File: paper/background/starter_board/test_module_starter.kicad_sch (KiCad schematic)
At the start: 14 parts, among them J1 Barrel_Jack_12V, M1 ERM_Motor, M2 Stepper_4wire, M3 Servo_3pin, U1 D24V22F5_Buck, U2 Pi_Pico_W, U3 DRV2605L_Breakout, U4 DRV8871_Breakout, U5 Tic_T500

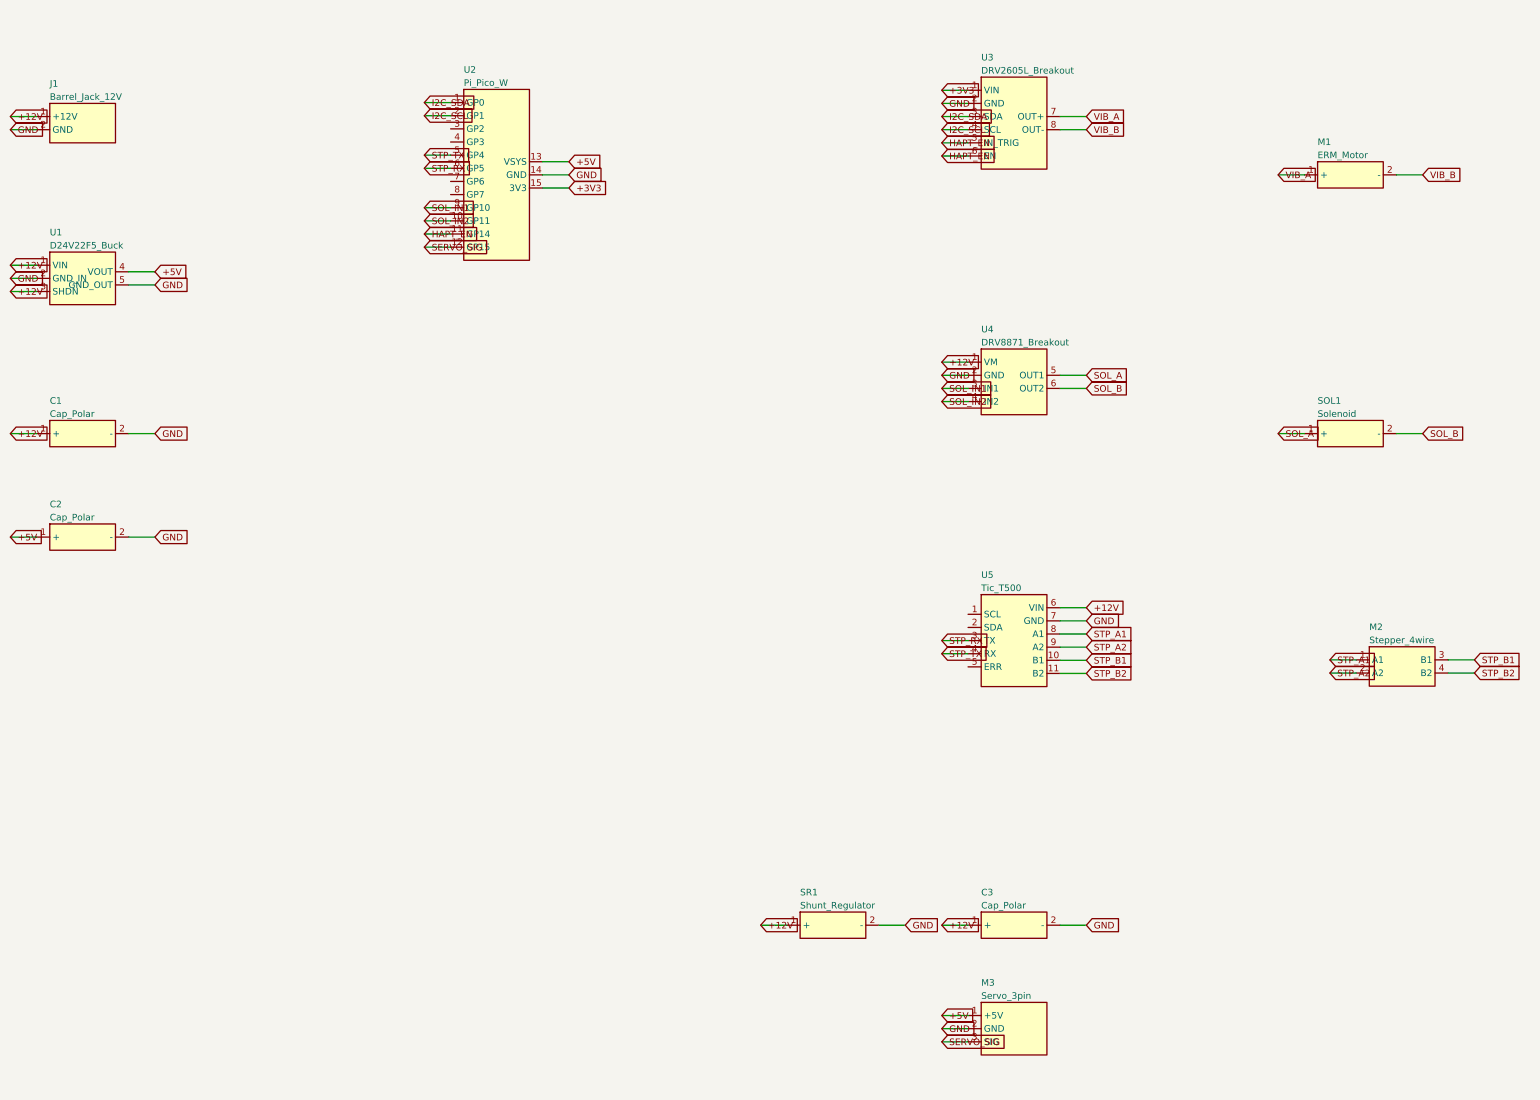
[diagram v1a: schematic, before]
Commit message: Fix starter-board pin counts to match real parts (Pico W 15→40, etc.)
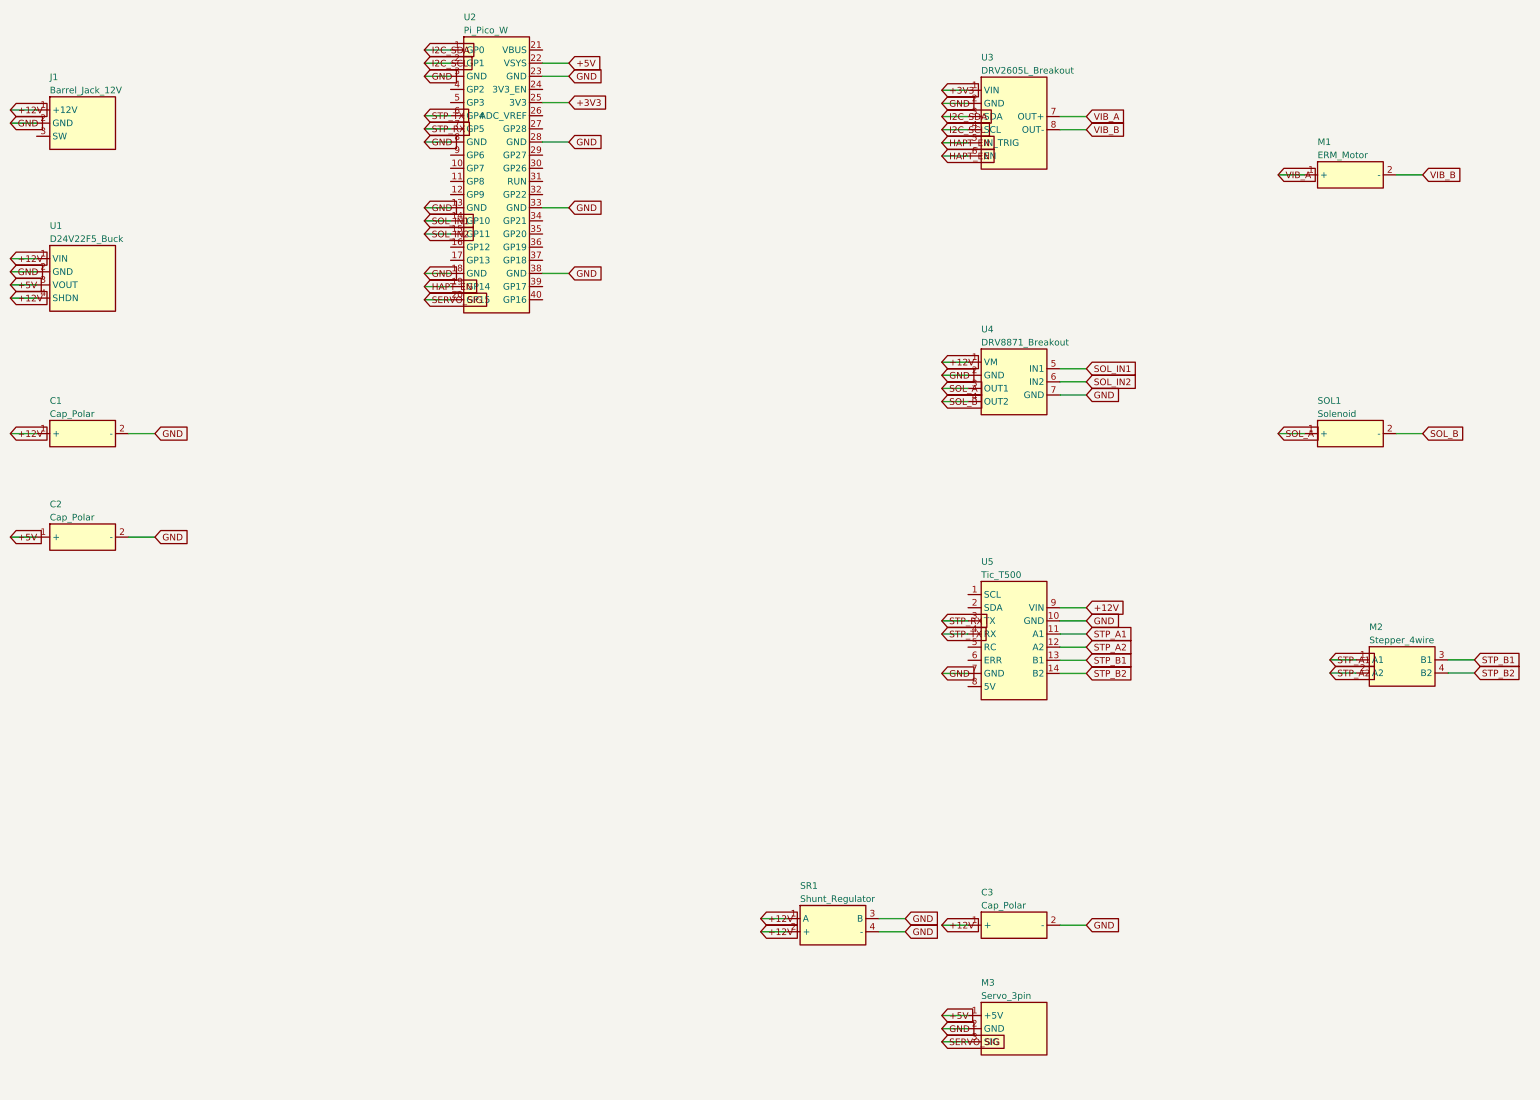
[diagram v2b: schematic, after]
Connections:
- net +12V: now also SR1.2 (+), U1.4 (SHDN), U5.9 (VIN); no longer U1.3 (SHDN), U5.6 (VIN)
- net +3V3: now also U2.25 (3V3); no longer U2.15 (3V3)
- net +5V: now also U1.3 (VOUT), U2.22 (VSYS); no longer U1.4 (VOUT), U2.13 (VSYS)
- net GND: now also SR1.3 (B), SR1.4 (-), U2.13 (GND), U2.18 (GND), U2.23 (GND), U2.28 (GND), U2.3 (GND), U2.33 (GND), U2.38 (GND), U2.8 (GND), U4.7 (GND), U5.10 (GND); no longer SR1.2 (-), U1.5 (GND_OUT), U2.14 (GND)
- net HAPT_EN: now also U2.19 (GP14); no longer U2.11 (GP14)
- net SERVO_SIG: now also U2.20 (GP15); no longer U2.12 (GP15)
- net SOL_A: now also U4.3 (OUT1); no longer U4.5 (OUT1)
- net SOL_B: now also U4.4 (OUT2); no longer U4.6 (OUT2)
- net SOL_IN1: now also U2.14 (GP10), U4.5 (IN1); no longer U2.9 (GP10), U4.3 (IN1)
- net SOL_IN2: now also U2.15 (GP11), U4.6 (IN2); no longer U2.10 (GP11), U4.4 (IN2)
- net STP_A1: now also U5.11 (A1); no longer U5.8 (A1)
- net STP_A2: now also U5.12 (A2); no longer U5.9 (A2)
- net STP_B1: now also U5.13 (B1); no longer U5.10 (B1)
- net STP_B2: now also U5.14 (B2); no longer U5.11 (B2)
- net STP_RX: now also U2.7 (GP5); no longer U2.6 (GP5)
- net STP_TX: now also U2.6 (GP4); no longer U2.5 (GP4)

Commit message: Swap starter-board placeholder pads for real KiCad library footprints
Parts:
- C1, C2, C3: footprint (none) -> Capacitor_THT:CP_Radial_D8.0mm_P3.50mm
- J1: footprint (none) -> Connector_BarrelJack:BarrelJack_Horizontal
- M1, SOL1: footprint (none) -> Connector_PinHeader_2.54mm:PinHeader_1x02_P2.54mm_Vertical
- M2: footprint (none) -> Connector_PinHeader_2.54mm:PinHeader_1x04_P2.54mm_Vertical
- M3: footprint (none) -> Connector_PinHeader_2.54mm:PinHeader_1x03_P2.54mm_Vertical
- SR1: footprint (none) -> powder_doser_parts:Shunt_Regulator
- U1: footprint (none) -> powder_doser_parts:D24V22F5_Buck
- U2: footprint (none) -> powder_doser_parts:Pi_Pico_W
- U3: footprint (none) -> powder_doser_parts:DRV2605L_Breakout
- U4: footprint (none) -> powder_doser_parts:DRV8871_Breakout
- U5: footprint (none) -> powder_doser_parts:Tic_T500
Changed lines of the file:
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@@
     (property "Value" "Barrel_Jack_12V" (id 1) (at 23.65 33.65 0)
       (effects (font (size 1.27 1.27)) (justify left)))
-    (property "Footprint" "" (id 2) (at 30 40 0)
+    (property "Footprint" "Connector_BarrelJack:BarrelJack_Horizontal" (id 2) (at 30 40 0)
       (effects (font (size 1.27 1.27)) hide))
     (property "Datasheet" "" (id 3) (at 30 40 0)
@@
     (property "Value" "D24V22F5_Buck" (id 1) (at 23.65 62.38 0)
       (effects (font (size 1.27 1.27)) (justify left)))
-    (property "Footprint" "" (id 2) (at 30 70 0)
+    (property "Footprint" "powder_doser_parts:D24V22F5_Buck" (id 2) (at 30 70 0)
       (effects (font (size 1.27 1.27)) hide))
     (property "Datasheet" "" (id 3) (at 30 70 0)
@@
     (property "Value" "Cap_Polar" (id 1) (at 23.65 96.19 0)
       (effects (font (size 1.27 1.27)) (justify left)))
-    (property "Footprint" "" (id 2) (at 30 100 0)
+    (property "Footprint" "Capacitor_THT:CP_Radial_D8.0mm_P3.50mm" (id 2) (at 30 100 0)
       (effects (font (size 1.27 1.27)) hide))
     (property "Datasheet" "" (id 3) (at 30 100 0)
@@
     (property "Value" "Cap_Polar" (id 1) (at 23.65 116.19 0)
       (effects (font (size 1.27 1.27)) (justify left)))
-    (property "Footprint" "" (id 2) (at 30 120 0)
+    (property "Footprint" "Capacitor_THT:CP_Radial_D8.0mm_P3.50mm" (id 2) (at 30 120 0)
       (effects (font (size 1.27 1.27)) hide))
     (property "Datasheet" "" (id 3) (at 30 120 0)
@@
     (property "Value" "Pi_Pico_W" (id 1) (at 103.65 22.06 0)
       (effects (font (size 1.27 1.27)) (justify left)))
-    (property "Footprint" "" (id 2) (at 110 50 0)
+    (property "Footprint" "powder_doser_parts:Pi_Pico_W" (id 2) (at 110 50 0)
       (effects (font (size 1.27 1.27)) hide))
     (property "Datasheet" "" (id 3) (at 110 50 0)
@@
     (property "Value" "DRV2605L_Breakout" (id 1) (at 203.65 29.84 0)
       (effects (font (size 1.27 1.27)) (justify left)))
-    (property "Footprint" "" (id 2) (at 210 40 0)
+    (property "Footprint" "powder_doser_parts:DRV2605L_Breakout" (id 2) (at 210 40 0)
       (effects (font (size 1.27 1.27)) hide))
     (property "Datasheet" "" (id 3) (at 210 40 0)
@@
     (property "Value" "ERM_Motor" (id 1) (at 268.65 46.19 0)
       (effects (font (size 1.27 1.27)) (justify left)))
-    (property "Footprint" "" (id 2) (at 275 50 0)
+    (property "Footprint" "Connector_PinHeader_2.54mm:PinHeader_1x02_P2.54mm_Vertical" (id 2) (at 275 50 0)
       (effects (font (size 1.27 1.27)) hide))
     (property "Datasheet" "" (id 3) (at 275 50 0)
@@
     (property "Value" "DRV8871_Breakout" (id 1) (at 203.65 82.38 0)
       (effects (font (size 1.27 1.27)) (justify left)))
-    (property "Footprint" "" (id 2) (at 210 90 0)
+    (property "Footprint" "powder_doser_parts:DRV8871_Breakout" (id 2) (at 210 90 0)
       (effects (font (size 1.27 1.27)) hide))
     (property "Datasheet" "" (id 3) (at 210 90 0)
@@
     (property "Value" "Solenoid" (id 1) (at 268.65 96.19 0)
       (effects (font (size 1.27 1.27)) (justify left)))
-    (property "Footprint" "" (id 2) (at 275 100 0)
+    (property "Footprint" "Connector_PinHeader_2.54mm:PinHeader_1x02_P2.54mm_Vertical" (id 2) (at 275 100 0)
       (effects (font (size 1.27 1.27)) hide))
     (property "Datasheet" "" (id 3) (at 275 100 0)
@@
     (property "Value" "Tic_T500" (id 1) (at 203.65 127.3 0)
       (effects (font (size 1.27 1.27)) (justify left)))
-    (property "Footprint" "" (id 2) (at 210 140 0)
+    (property "Footprint" "powder_doser_parts:Tic_T500" (id 2) (at 210 140 0)
       (effects (font (size 1.27 1.27)) hide))
     (property "Datasheet" "" (id 3) (at 210 140 0)
@@
     (property "Value" "Cap_Polar" (id 1) (at 203.65 191.19 0)
       (effects (font (size 1.27 1.27)) (justify left)))
-    (property "Footprint" "" (id 2) (at 210 195 0)
+    (property "Footprint" "Capacitor_THT:CP_Radial_D8.0mm_P3.50mm" (id 2) (at 210 195 0)
       (effects (font (size 1.27 1.27)) hide))
     (property "Datasheet" "" (id 3) (at 210 195 0)
@@
     (property "Value" "Shunt_Regulator" (id 1) (at 168.65 189.92 0)
       (effects (font (size 1.27 1.27)) (justify left)))
-    (property "Footprint" "" (id 2) (at 175 195 0)
+    (property "Footprint" "powder_doser_parts:Shunt_Regulator" (id 2) (at 175 195 0)
       (effects (font (size 1.27 1.27)) hide))
     (property "Datasheet" "" (id 3) (at 175 195 0)
@@
     (property "Value" "Stepper_4wire" (id 1) (at 278.65 139.92 0)
       (effects (font (size 1.27 1.27)) (justify left)))
-    (property "Footprint" "" (id 2) (at 285 145 0)
+    (property "Footprint" "Connector_PinHeader_2.54mm:PinHeader_1x04_P2.54mm_Vertical" (id 2) (at 285 145 0)
       (effects (font (size 1.27 1.27)) hide))
     (property "Datasheet" "" (id 3) (at 285 145 0)
@@
     (property "Value" "Servo_3pin" (id 1) (at 203.65 208.65 0)
       (effects (font (size 1.27 1.27)) (justify left)))
-    (property "Footprint" "" (id 2) (at 210 215 0)
+    (property "Footprint" "Connector_PinHeader_2.54mm:PinHeader_1x03_P2.54mm_Vertical" (id 2) (at 210 215 0)
       (effects (font (size 1.27 1.27)) hide))
     (property "Datasheet" "" (id 3) (at 210 215 0)
